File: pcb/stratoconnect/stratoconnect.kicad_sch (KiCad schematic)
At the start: 29 parts, among them J1 Conn_Coaxial, J2 Conn_02x03_Odd_Even, J3 Conn_01x05_Male, J4 Conn_01x02_Male, J5 Conn_01x03_Male, SW1 SW_SPST, U1 RF4463f30, U2 ATmega328PB-A, Y1 CSTNE16M0V530000R0

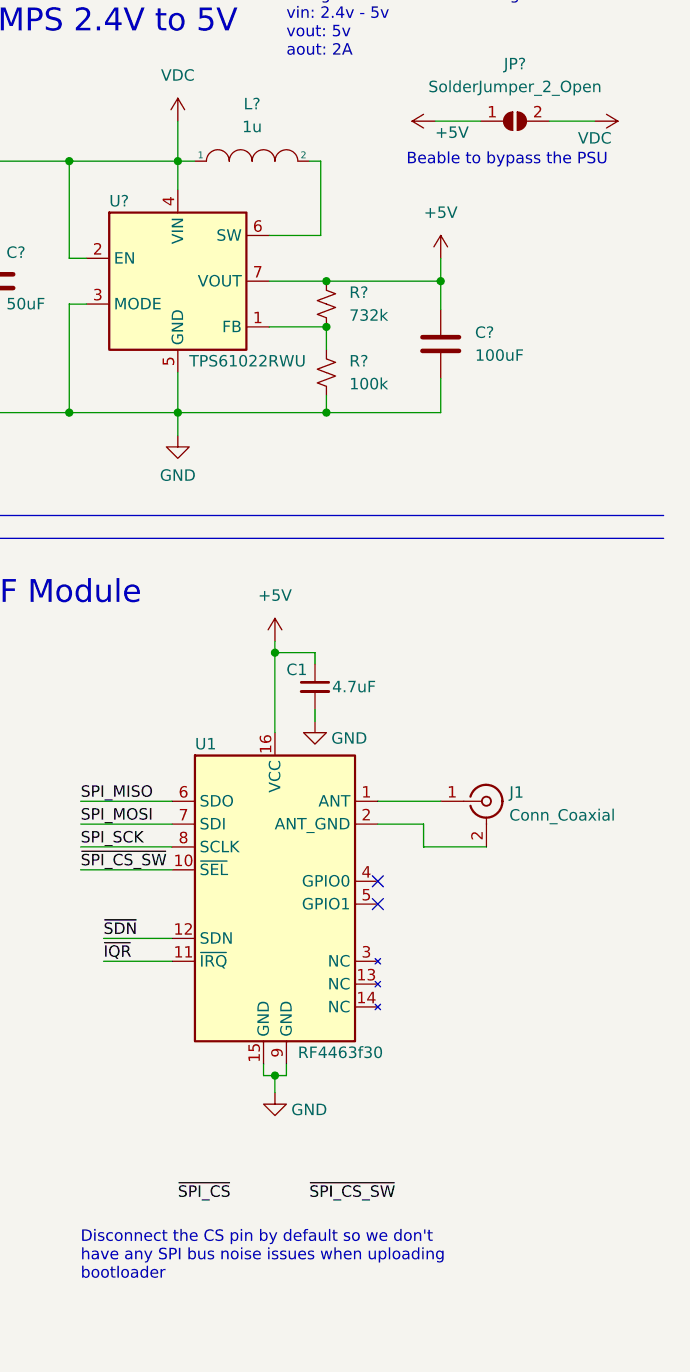
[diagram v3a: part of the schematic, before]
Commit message: add some more annotations to the smps
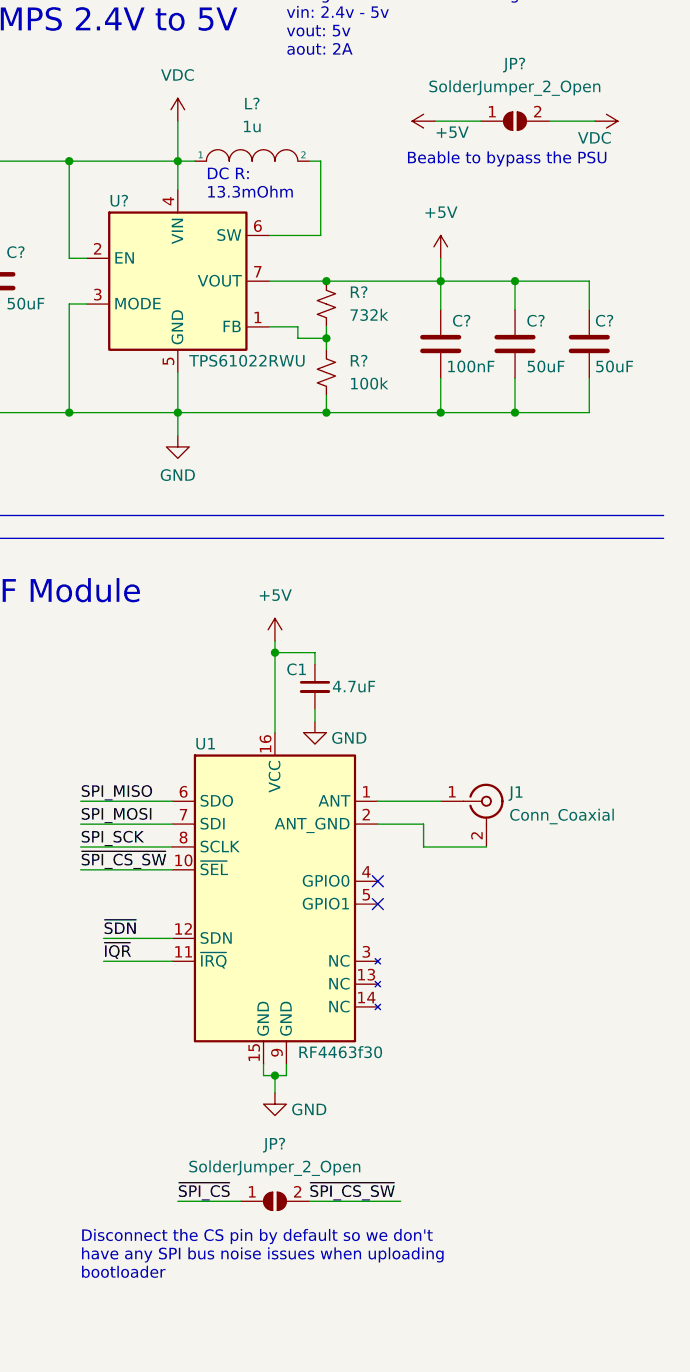
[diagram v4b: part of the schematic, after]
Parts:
- added C? (x2): 50uF, symbol Device:C
- added JP?: SolderJumper_2_Open, symbol Jumper:SolderJumper_2_Open
- C?: value 100uF -> 100nF
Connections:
- net +5V: now also C?.1, C?.1
- net GND: now also C?.2, C?.2
- net ~{SPI_CS_SW}: now also JP?.2 (B)
- net ~{SPI_CS}: now also JP?.1 (A)
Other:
- note added: "DC R: 13.3mOhm"
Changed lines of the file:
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@@
   (junction (at 241.935 134.62) (diameter 0) (color 0 0 0 0)
   )
+  (junction (at 268.605 46.355) (diameter 0) (color 0 0 0 0)
+  )
   (junction (at 219.075 33.02) (diameter 0) (color 0 0 0 0)
   )
-  (junction (at 247.65 51.435) (diameter 0) (color 0 0 0 0)
+  (junction (at 247.65 52.705) (diameter 0) (color 0 0 0 0)
+  )
+  (junction (at 260.35 60.96) (diameter 0) (color 0 0 0 0)
   )
   (junction (at 157.48 39.37) (diameter 0) (color 0 0 0 0)
   )
   (junction (at 219.075 60.96) (diameter 0) (color 0 0 0 0)
+  )
+  (junction (at 268.605 60.96) (diameter 0) (color 0 0 0 0)
   )
   (junction (at 85.09 74.93) (diameter 0) (color 0 0 0 0)
@@
     (stroke (width 0) (type default) (color 0 0 0 0))
   )
+  (wire (pts (xy 268.605 60.96) (xy 276.86 60.96))
+    (stroke (width 0) (type default) (color 0 0 0 0))
+  )
   (wire (pts (xy 168.91 105.41) (xy 168.91 106.68))
     (stroke (width 0) (type default) (color 0 0 0 0))
@@
     (stroke (width 0) (type default) (color 0 0 0 0))
   )
+  (wire (pts (xy 247.65 60.96) (xy 260.35 60.96))
+    (stroke (width 0) (type default) (color 0 0 0 0))
+  )
+  (wire (pts (xy 244.475 51.435) (xy 244.475 52.705))
+    (stroke (width 0) (type default) (color 0 0 0 0))
+  )
+  (wire (pts (xy 260.35 60.96) (xy 268.605 60.96))
+    (stroke (width 0) (type default) (color 0 0 0 0))
+  )
+  (wire (pts (xy 276.86 46.355) (xy 276.86 49.53))
+    (stroke (width 0) (type default) (color 0 0 0 0))
+  )
   (wire (pts (xy 92.71 111.76) (xy 97.79 111.76))
     (stroke (width 0) (type default) (color 0 0 0 0))
@@
     (stroke (width 0) (type default) (color 0 0 0 0))
   )
+  (wire (pts (xy 71.12 157.48) (xy 71.12 159.385))
+    (stroke (width 0) (type default) (color 0 0 0 0))
+  )
+  (wire (pts (xy 154.94 150.495) (xy 163.83 150.495))
+    (stroke (width 0) (type default) (color 0 0 0 0))
+  )
+  (wire (pts (xy 80.01 66.04) (xy 85.09 66.04))
+    (stroke (width 0) (type default) (color 0 0 0 0))
+  )
   (wire (pts (xy 247.65 46.355) (xy 260.35 46.355))
     (stroke (width 0) (type default) (color 0 0 0 0))
   )
-  (wire (pts (xy 71.12 157.48) (xy 71.12 159.385))
-    (stroke (width 0) (type default) (color 0 0 0 0))
-  )
-  (wire (pts (xy 154.94 150.495) (xy 163.83 150.495))
-    (stroke (width 0) (type default) (color 0 0 0 0))
-  )
-  (wire (pts (xy 80.01 66.04) (xy 85.09 66.04))
-    (stroke (width 0) (type default) (color 0 0 0 0))
-  )
   (polyline (pts (xy 204.47 165.735) (xy 204.47 74.93))
     (stroke (width 0) (type default) (color 0 0 0 0))
@@
     (stroke (width 0) (type default) (color 0 0 0 0))
   )
-  (wire (pts (xy 247.65 51.435) (xy 247.65 53.975))
-    (stroke (width 0) (type default) (color 0 0 0 0))
-  )
   (polyline (pts (xy 204.47 74.93) (xy 139.065 74.93))
     (stroke (width 0) (type default) (color 0 0 0 0))
@@
     (stroke (width 0) (type default) (color 0 0 0 0))
   )
+  (wire (pts (xy 245.745 148.59) (xy 255.905 148.59))
+    (stroke (width 0) (type default) (color 0 0 0 0))
+  )
   (wire (pts (xy 231.14 60.96) (xy 247.65 60.96))
     (stroke (width 0) (type default) (color 0 0 0 0))
@@
     (stroke (width 0) (type default) (color 0 0 0 0))
   )
+  (wire (pts (xy 231.14 148.59) (xy 238.125 148.59))
+    (stroke (width 0) (type default) (color 0 0 0 0))
+  )
   (wire (pts (xy 46.355 132.08) (xy 55.88 132.08))
     (stroke (width 0) (type default) (color 0 0 0 0))
@@
     (stroke (width 0) (type default) (color 0 0 0 0))
   )
+  (wire (pts (xy 260.35 46.355) (xy 268.605 46.355))
+    (stroke (width 0) (type default) (color 0 0 0 0))
+  )
   (wire (pts (xy 243.205 133.35) (xy 243.205 134.62))
     (stroke (width 0) (type default) (color 0 0 0 0))
@@
     (stroke (width 0) (type default) (color 0 0 0 0))
   )
-  (wire (pts (xy 247.65 60.96) (xy 260.35 60.96))
-    (stroke (width 0) (type default) (color 0 0 0 0))
-  )
   (wire (pts (xy 241.935 134.62) (xy 241.935 136.525))
     (stroke (width 0) (type default) (color 0 0 0 0))
   )
+  (wire (pts (xy 268.605 57.15) (xy 268.605 60.96))
+    (stroke (width 0) (type default) (color 0 0 0 0))
+  )
   (wire (pts (xy 219.075 33.02) (xy 219.075 43.815))
     (stroke (width 0) (type default) (color 0 0 0 0))
@@
     (stroke (width 0) (type default) (color 0 0 0 0))
   )
-  (wire (pts (xy 241.3 51.435) (xy 247.65 51.435))
+  (wire (pts (xy 268.605 46.355) (xy 268.605 49.53))
     (stroke (width 0) (type default) (color 0 0 0 0))
   )
@@
     (stroke (width 0) (type default) (color 0 0 0 0))
   )
+  (wire (pts (xy 268.605 46.355) (xy 276.86 46.355))
+    (stroke (width 0) (type default) (color 0 0 0 0))
+  )
+  (wire (pts (xy 247.65 51.435) (xy 247.65 52.705))
+    (stroke (width 0) (type default) (color 0 0 0 0))
+  )
   (wire (pts (xy 73.66 81.28) (xy 73.66 78.74))
     (stroke (width 0) (type default) (color 0 0 0 0))
@@
     (stroke (width 0) (type default) (color 0 0 0 0))
   )
+  (wire (pts (xy 276.86 57.15) (xy 276.86 60.96))
+    (stroke (width 0) (type default) (color 0 0 0 0))
+  )
   (wire (pts (xy 55.88 88.9) (xy 53.975 88.9))
     (stroke (width 0) (type default) (color 0 0 0 0))
@@
     (stroke (width 0) (type default) (color 0 0 0 0))
   )
+  (wire (pts (xy 244.475 52.705) (xy 247.65 52.705))
+    (stroke (width 0) (type default) (color 0 0 0 0))
+  )
   (wire (pts (xy 85.09 73.66) (xy 85.09 74.93))
     (stroke (width 0) (type default) (color 0 0 0 0))
@@
     (stroke (width 0) (type default) (color 0 0 0 0))
   )
+  (wire (pts (xy 241.3 51.435) (xy 244.475 51.435))
+    (stroke (width 0) (type default) (color 0 0 0 0))
+  )
   (wire (pts (xy 241.3 46.355) (xy 247.65 46.355))
     (stroke (width 0) (type default) (color 0 0 0 0))
@@
   )
   (wire (pts (xy 240.665 133.35) (xy 240.665 134.62))
+    (stroke (width 0) (type default) (color 0 0 0 0))
+  )
+  (wire (pts (xy 247.65 52.705) (xy 247.65 53.975))
     (stroke (width 0) (type default) (color 0 0 0 0))
   )
@@
     (effects (font (size 2.54 2.54)) (justify left bottom))
   )
+  (text "DC R:\n13.3mOhm " (at 234.315 37.465 0)
+    (effects (font (size 1.27 1.27)) (justify left bottom))
+  )
   (text "SMPS 2.4V to 5V" (at 208.915 19.05 0)
     (effects (font (size 2.54 2.54)) (justify left bottom))
@@
     )
     (pin "1")
+  )
+  (symbol (lib_id "Jumper:SolderJumper_2_Open") (at 241.935 148.59 0) (unit 1)
+    (in_bom yes) (on_board yes) (fields_autoplaced)
+    (property "Reference" "JP?" (id 0) (at 241.935 142.24 0))
+    (property "Value" "SolderJumper_2_Open" (id 1) (at 241.935 144.78 0))
+    (property "Footprint" "" (id 2) (at 241.935 148.59 0)
+      (effects (font (size 1.27 1.27)) hide)
+    )
+    (property "Datasheet" "~" (id 3) (at 241.935 148.59 0)
+      (effects (font (size 1.27 1.27)) hide)
+    )
+    (pin "1")
+    (pin "2")
   )
   (symbol (lib_id "Switch:SW_SPST") (at 151.13 39.37 0) (unit 1)
@@
   )
   (symbol (lib_id "Device:C") (at 260.35 53.34 0) (unit 1)
-    (in_bom yes) (on_board yes) (fields_autoplaced)
-    (property "Reference" "C?" (id 0) (at 264.16 52.0699 0)
-      (effects (font (size 1.27 1.27)) (justify left))
-    )
-    (property "Value" "100uF" (id 1) (at 264.16 54.6099 0)
+    (in_bom yes) (on_board yes)
+    (property "Reference" "C?" (id 0) (at 261.62 50.8 0)
+      (effects (font (size 1.27 1.27)) (justify left))
+    )
+    (property "Value" "100nF" (id 1) (at 260.985 55.88 0)
       (effects (font (size 1.27 1.27)) (justify left))
     )
@@
     (pin "7")
   )
+  (symbol (lib_id "Device:C") (at 276.86 53.34 0) (unit 1)
+    (in_bom yes) (on_board yes)
+    (property "Reference" "C?" (id 0) (at 277.495 50.8 0)
+      (effects (font (size 1.27 1.27)) (justify left))
+    )
+    (property "Value" "50uF" (id 1) (at 277.495 55.88 0)
+      (effects (font (size 1.27 1.27)) (justify left))
+    )
+    (property "Footprint" "" (id 2) (at 277.8252 57.15 0)
+      (effects (font (size 1.27 1.27)) hide)
+    )
+    (property "Datasheet" "~" (id 3) (at 276.86 53.34 0)
+      (effects (font (size 1.27 1.27)) hide)
+    )
+    (pin "1")
+    (pin "2")
+  )
   (symbol (lib_id "power:+3V3") (at 177.8 101.6 0) (unit 1)
     (in_bom yes) (on_board yes)
@@
     )
     (pin "1")
+  )
+  (symbol (lib_id "Device:C") (at 268.605 53.34 0) (unit 1)
+    (in_bom yes) (on_board yes)
+    (property "Reference" "C?" (id 0) (at 269.875 50.8 0)
+      (effects (font (size 1.27 1.27)) (justify left))
+    )
+    (property "Value" "50uF" (id 1) (at 269.875 55.88 0)
+      (effects (font (size 1.27 1.27)) (justify left))
+    )
+    (property "Footprint" "" (id 2) (at 269.5702 57.15 0)
+      (effects (font (size 1.27 1.27)) hide)
+    )
+    (property "Datasheet" "~" (id 3) (at 268.605 53.34 0)
+      (effects (font (size 1.27 1.27)) hide)
+    )
+    (pin "1")
+    (pin "2")
   )
   (symbol (lib_id "Connector_Generic:Conn_02x03_Odd_Even") (at 168.91 150.495 0) (unit 1)
@@
     )
     (path "/3f74c64e-f085-40aa-83ab-c6d1f7d3a1e9"
-      (reference "C?") (unit 1) (value "100uF") (footprint "")
+      (reference "C?") (unit 1) (value "100nF") (footprint "")
+    )
+    (path "/8daab3e3-bac4-47f0-80cf-c837ba611f67"
+      (reference "C?") (unit 1) (value "50uF") (footprint "")
     )
     (path "/92d3eeb8-e53e-4781-96b3-b24edf0af3bc"
       (reference "C?") (unit 1) (value "50uF") (footprint "")
     )
+    (path "/b8b9acc5-7bab-4c90-b293-8ccdd08d8014"
+      (reference "C?") (unit 1) (value "50uF") (footprint "")
+    )
     (path "/71b26196-b391-490d-b601-aacc855dc7a8"
       (reference "D?") (unit 1) (value "LED") (footprint "LED_SMD:LED_0805_2012Metric")
@@
       (reference "J5") (unit 1) (value "Conn_01x03_Male") (footprint "Connector_JST:JST_GH_BM03B-GHS-TBT_1x03-1MP_P1.25mm_Vertical")
     )
+    (path "/10ac7e32-ddb3-4b3b-9fea-3c221fce92d6"
+      (reference "JP?") (unit 1) (value "SolderJumper_2_Open") (footprint "")
+    )
     (path "/e9e153b3-936d-4c94-a787-9e9f29cb1ea5"

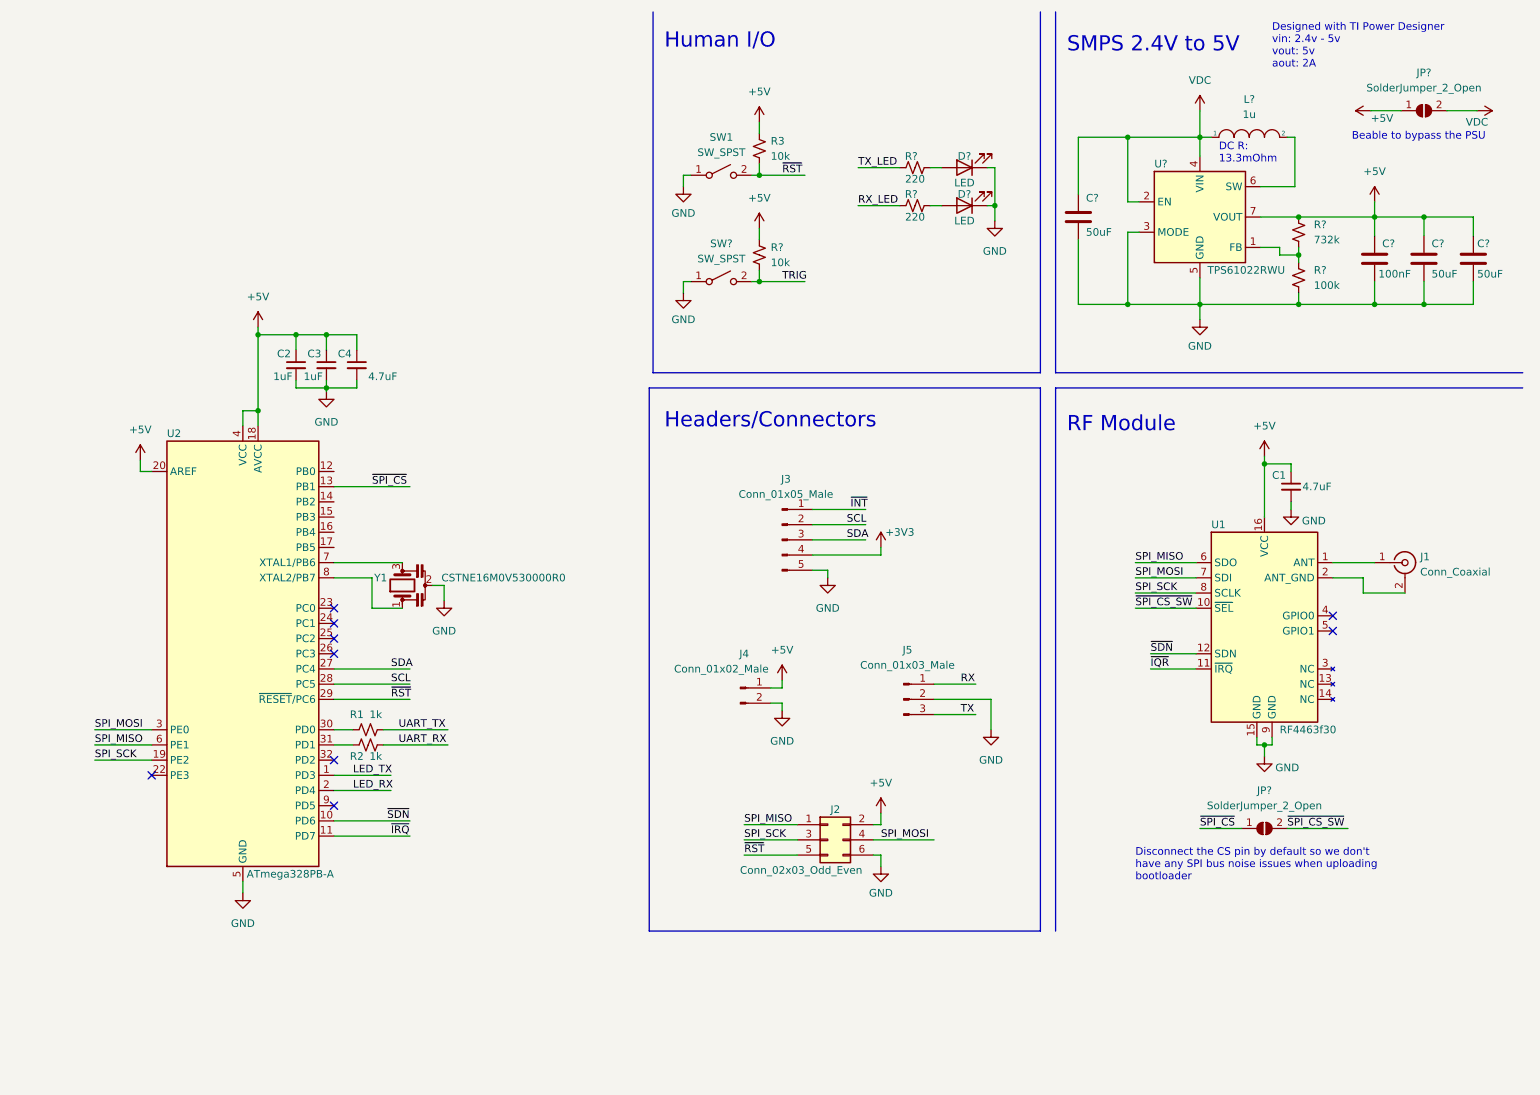
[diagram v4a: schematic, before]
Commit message: add 6060 Inductor foodprint
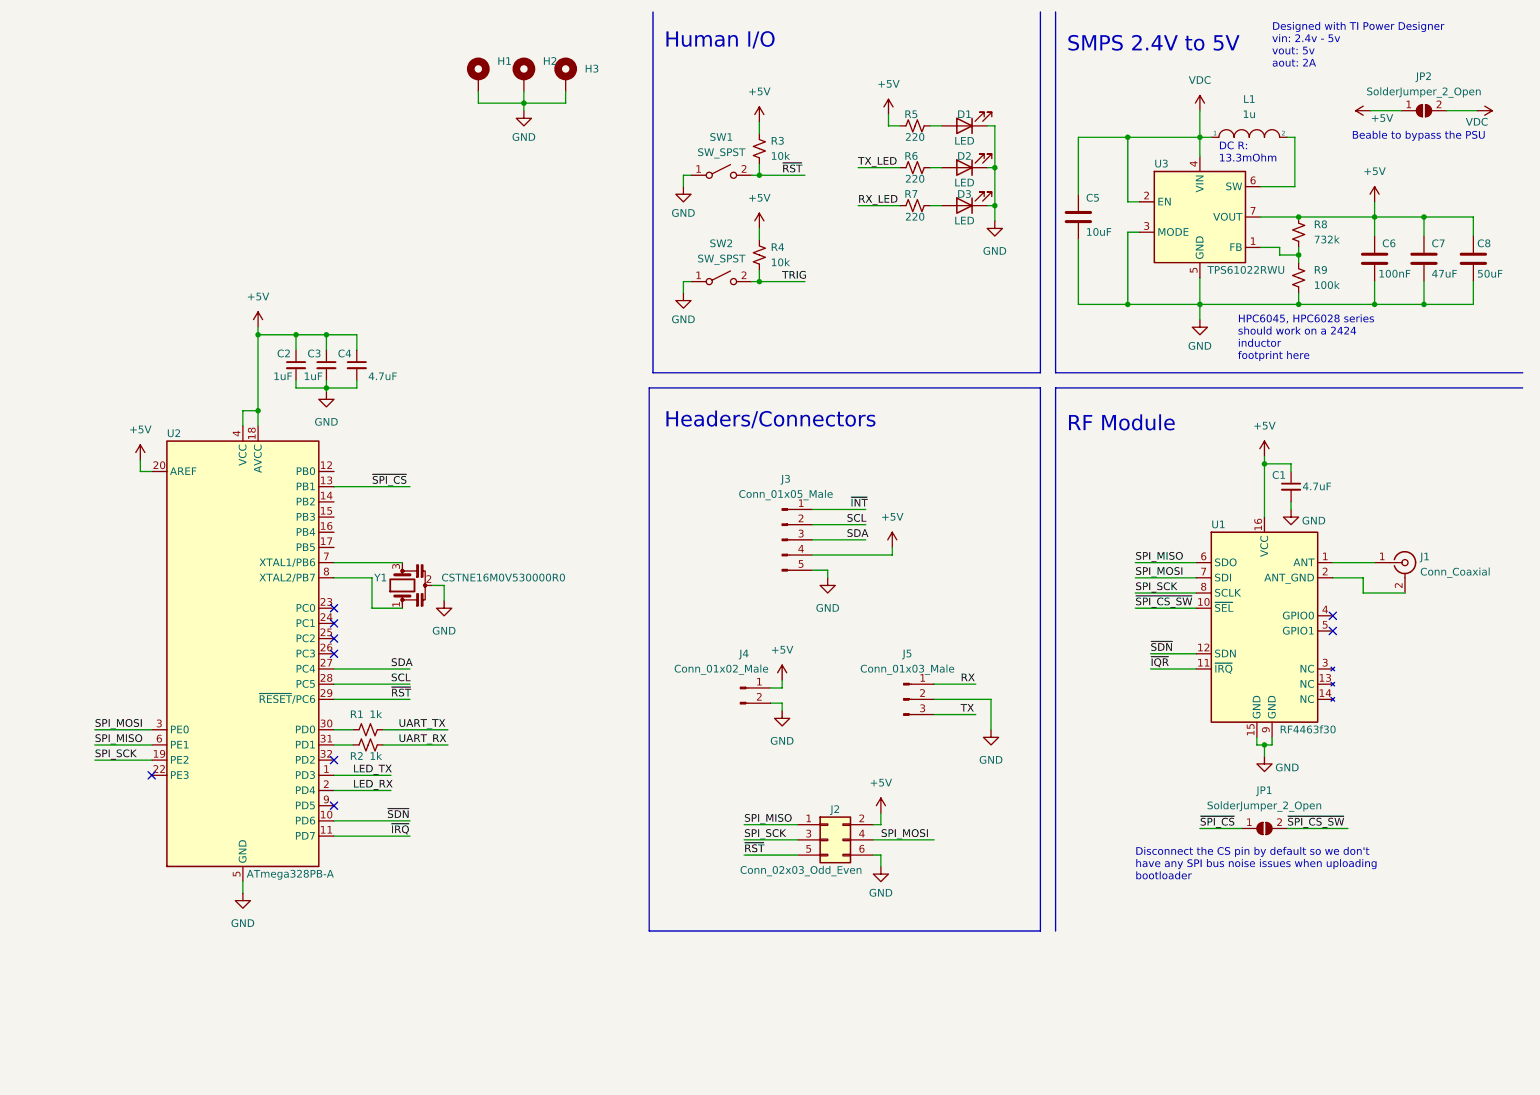
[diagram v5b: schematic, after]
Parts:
- added D1: LED, LED_SMD:LED_0603_1608Metric, symbol Device:LED
- added H1, H2: MountingHole_Pad, MountingHole:MountingHole_3.2mm_M3_Pad_Via, symbol Mechanical:MountingHole_Pad
- added H3: MountingHole_Pad, symbol Mechanical:MountingHole_Pad
- added R5: 220, Resistor_SMD:R_0603_1608Metric, symbol Device:R_Small_US
- C5: renamed from C?; value 50uF -> 10uF; footprint (none) -> Capacitor_SMD:C_0805_2012Metric
- C6: renamed from C?; footprint (none) -> Capacitor_SMD:C_0603_1608Metric
- C7: renamed from C?; value 50uF -> 47uF; footprint (none) -> Capacitor_SMD:CP_Elec_5x5.3
- C8: renamed from C?; footprint (none) -> Capacitor_SMD:CP_Elec_5x5.3
- D2, D3: renamed from D?; footprint LED_SMD:LED_0805_2012Metric -> LED_SMD:LED_0603_1608Metric
- J3: footprint Connector_JST:JST_GH_BM05B-GHS-TBT_1x05-1MP_P1.25mm_Vertical -> Connector_JST:JST_GH_SM05B-GHS-TB_1x05-1MP_P1.25mm_Horizontal
- J5: footprint Connector_JST:JST_GH_BM03B-GHS-TBT_1x03-1MP_P1.25mm_Vertical -> Connector_JST:JST_GH_SM03B-GHS-TB_1x03-1MP_P1.25mm_Horizontal
- JP1, JP2: renamed from JP?; footprint (none) -> Jumper:SolderJumper-2_P1.3mm_Open_RoundedPad1.0x1.5mm
- L1: renamed from L?; footprint (none) -> Inductor_SMD:L_2440_6060Metric
- R9: renamed from R?; footprint (none) -> Resistor_SMD:R_0805_2012Metric
- gave numbers to parts that had none: 6
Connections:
- net +3V3 is gone; now on net +5V: J3.4 (Pin_4)
- net +5V: now also R5.1
- net GND: now also D1.1 (K), H1.1, H2.1, H3.1
- new net: D1.2 (A), R5.2
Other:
- note added: "HPC6045, HPC6028 series should work on a 2424 inductor footprint here"
